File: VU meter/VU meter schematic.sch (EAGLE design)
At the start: 10 parts

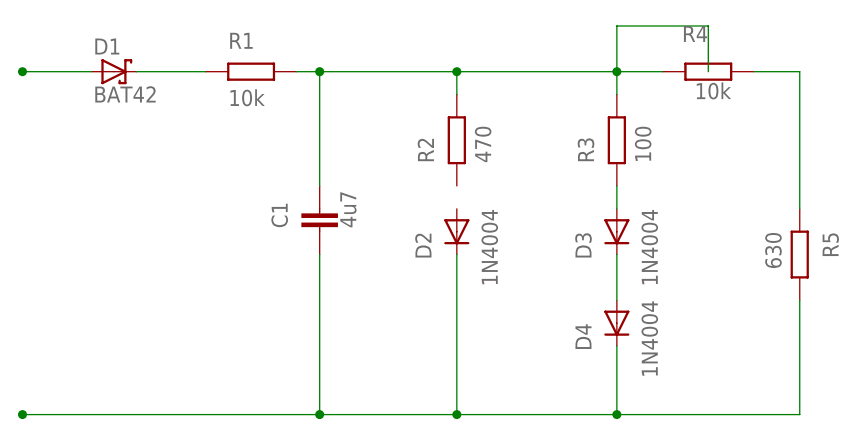
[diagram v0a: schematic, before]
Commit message: Update VU meter schematic.sch
Fixed some routing issues.
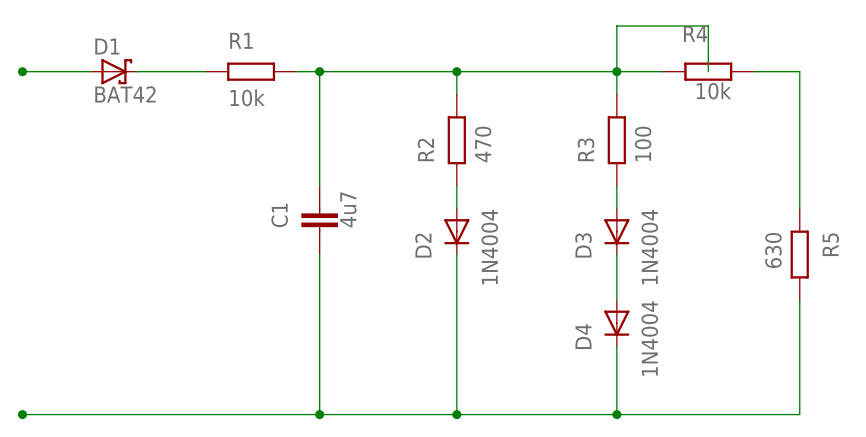
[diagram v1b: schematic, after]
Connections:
- new net N$8: D2.A, R2.1
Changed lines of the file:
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@@
+</segment>
+</net>
+<net name="N$8" class="0">
+<segment>
+<pinref part="R2" gate="G$1" pin="1"/>
+<pinref part="D2" gate="1" pin="A"/>
+<wire x1="66.04" y1="60.96" x2="66.04" y2="58.42" width="0.1524" layer="91"/>
 </segment>
 </net>
